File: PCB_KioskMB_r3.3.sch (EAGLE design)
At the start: 329 parts, among them IC1 ISL60002DIH325Z-TK, IC18 FT232RL, IC19 MCP6022-I/ST, IC2 SN65HVD12D, IC21 LTC1771EMS8, IC3 PIC24FJ256GA110-I/PT, IC4 PIC10F200T-I/OT, IC5 LM75ADP, IC6 24LC32A-I/MS, IC7 PCF2123TS/1-T, IC8 M25P16-VMN6P, IC9 LM3405AXMK/NOPB, J1 DF11-10DP-2DSA(01), J10 CCM03-3504LFT-NR, J14 3-641215-2, J15 1990834, J16 1990737, J17 14011213102000, J18 14011213102000, J19 14011213102000, J30 22-11-2072, J4 3-641215-2, J45 3-641215-4, J47 DF11-10DP-2DSA(01), J48 3-641215-2, J49 3-641215-2, J50 0039301040, J7 SS-6566-NF, J8 TSW-108-07-G-D, J9 SS-6566-NF, Q14 MAX9938HEUK, Q15 SI4564DY, Q16 CSD87331Q3D, Q18 SI4564DY, Q19 CSD87331Q3D, Q2 FDC6330L, Q20 IPD30N06S2L-23, Q21 IPD30N06S2L-23, Q23 FDN352AP, Q24 BSS138, Q3 SR3.3.TCT, Q4 7B-28.63636MAAJ-T, Q5 FDC6330L, Q6 CM519 32.768KDZF-UT, Q7 SSM6P49NU,LFPZ, U1 LTC1955, U2 LE33, U3 ADS1015, U6 TPS43061, U7 TPS43061, U8 TPA3111D1PWP, U9 OPA322SAIDBVT, X1 FH12-10S-0.5S1.00MM, X2 MINI-USB_4P-85-32004-10X

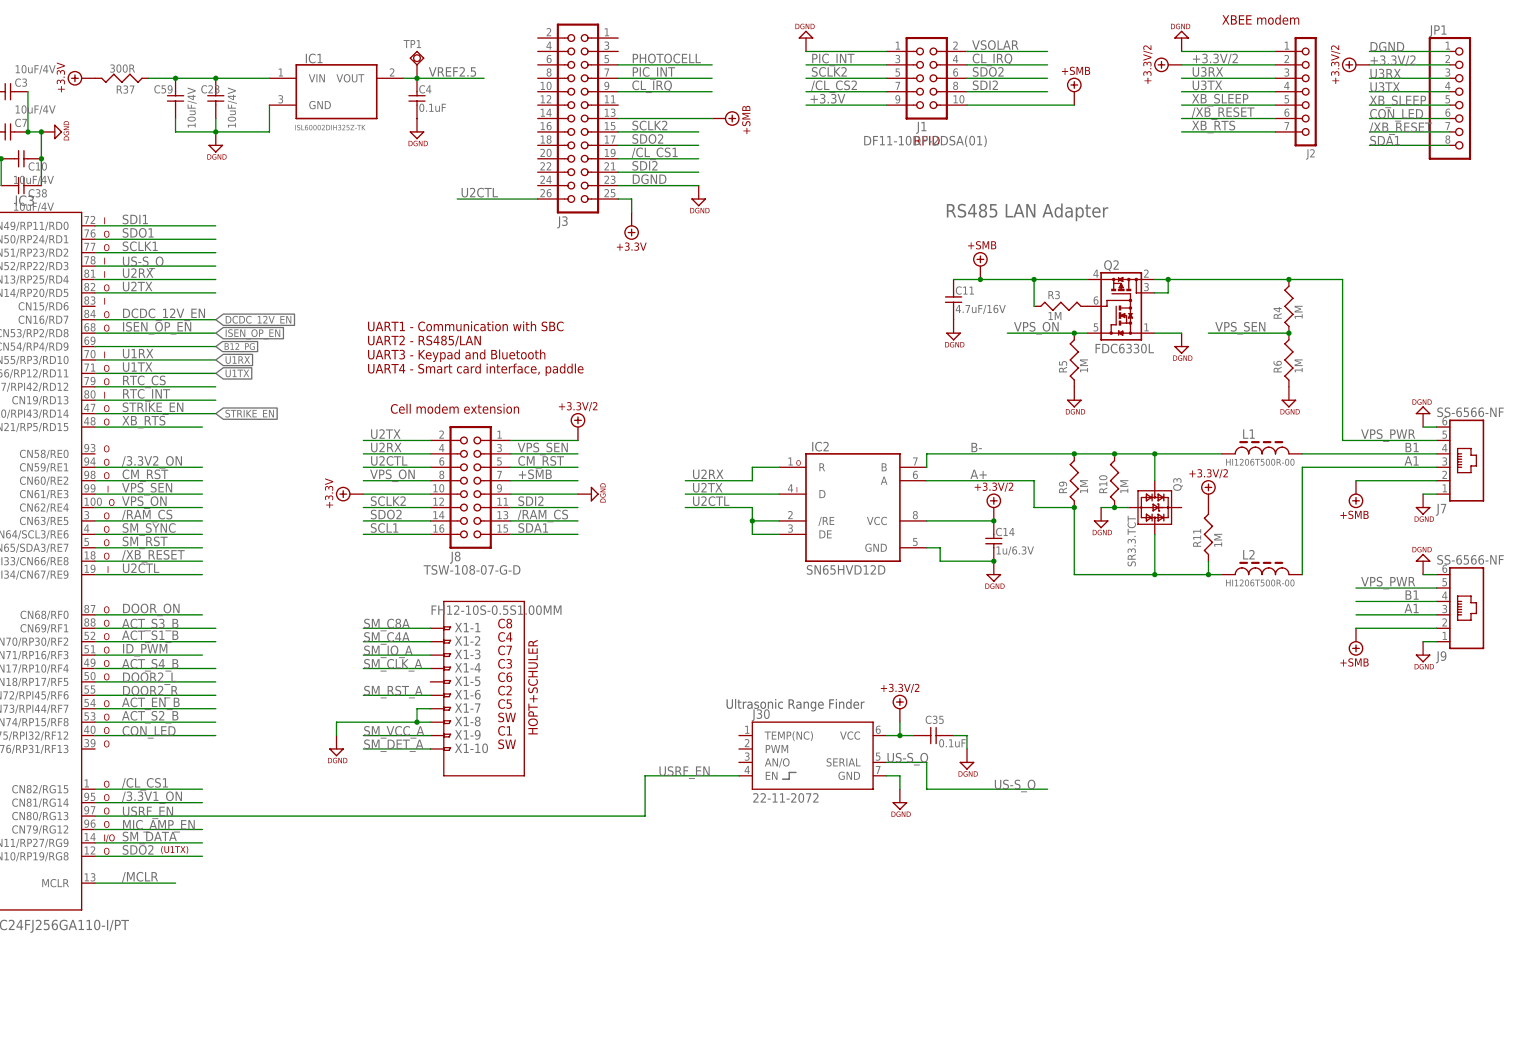
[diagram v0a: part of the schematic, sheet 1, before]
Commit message: added .png of connectors.
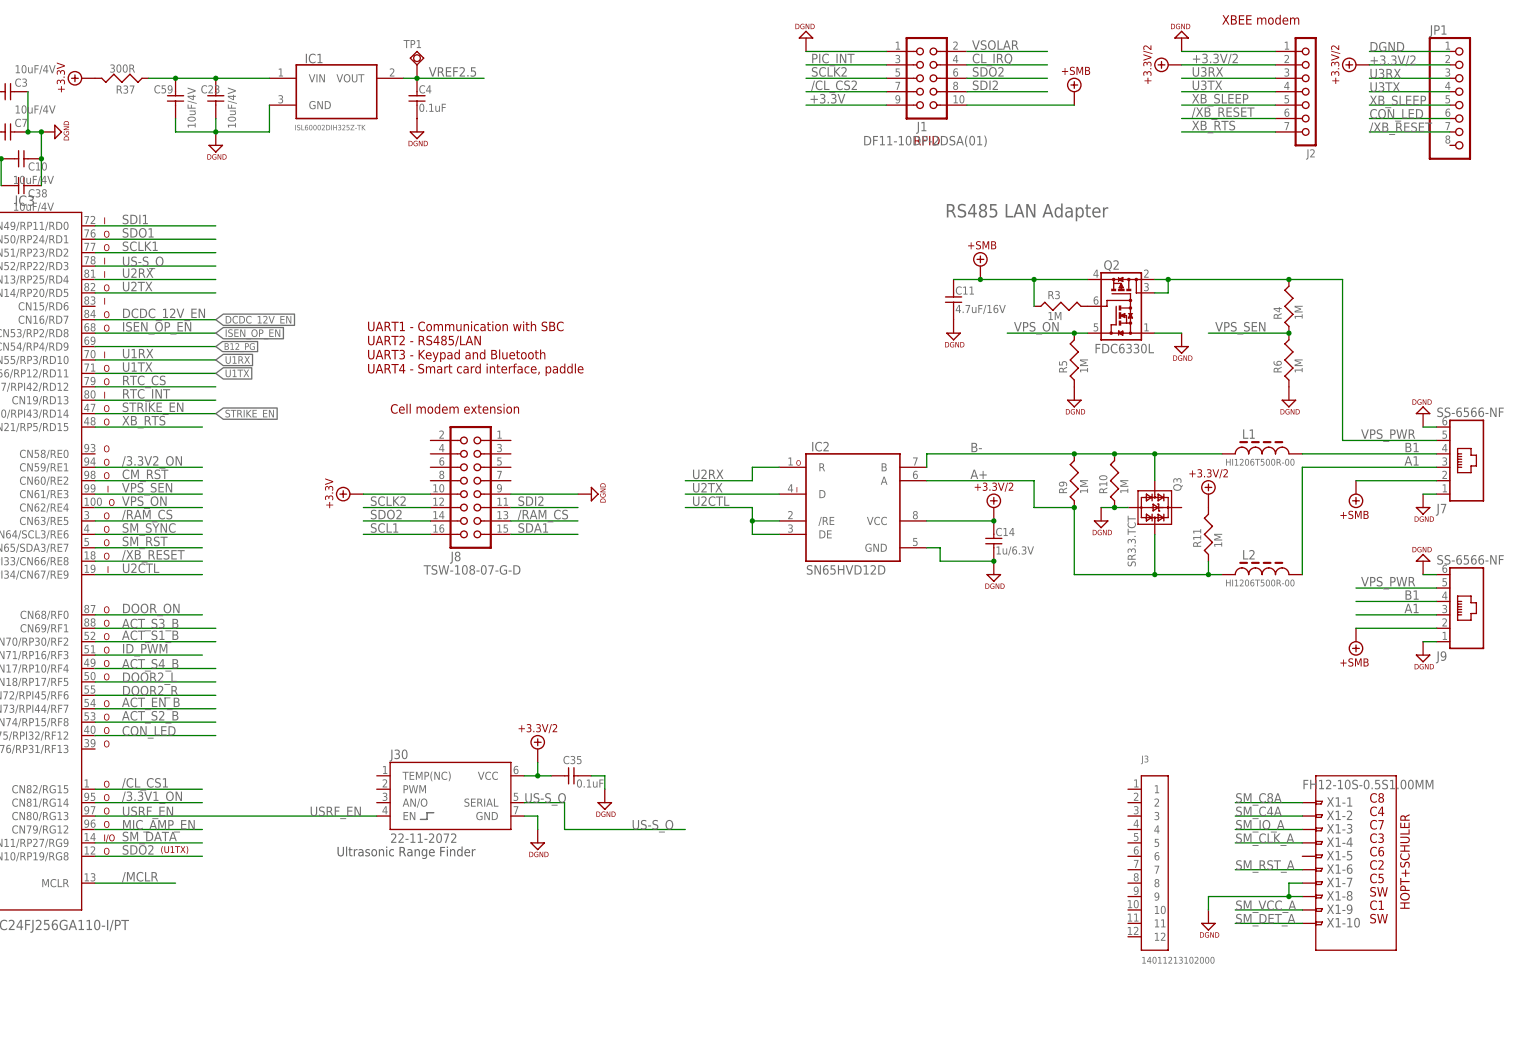
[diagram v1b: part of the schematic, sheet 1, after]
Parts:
- J3: value (none) -> 14011213102000; device CON-pinHeader-AON:MA13-2 -> elock_lib:14011213102000
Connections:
- net +3.3V: no longer J3.25
- net +3.3V/2: no longer J8.1
- net +SMB: no longer J3.13, J8.7
- net /CL_CS1: no longer J3.19
- net CL_IRQ: no longer J3.9
- net CM_RST: no longer J8.5
- net DGND: no longer J3.23
- net PHOTOCELL: no longer J3.5
- net PIC_INT: no longer J3.7
- net SCLK2: no longer J3.15
- net SDA1: no longer JP1.8
- net SDI2: no longer J3.21
- net SDO2: no longer J3.17
- net U2CTL: no longer J3.26, J8.6
- net U2RX: no longer J8.4
- net U2TX: no longer J8.2
- net VPS_ON: no longer J8.8
- net VPS_SEN: no longer J8.3
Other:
- moved on the sheet: C35, J16, J17, J18, J19, J30, X1-1, X1-10, X1-2, X1-3, X1-4, X1-5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
